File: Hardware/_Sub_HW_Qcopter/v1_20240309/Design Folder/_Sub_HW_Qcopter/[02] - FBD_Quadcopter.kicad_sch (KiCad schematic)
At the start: 0 parts

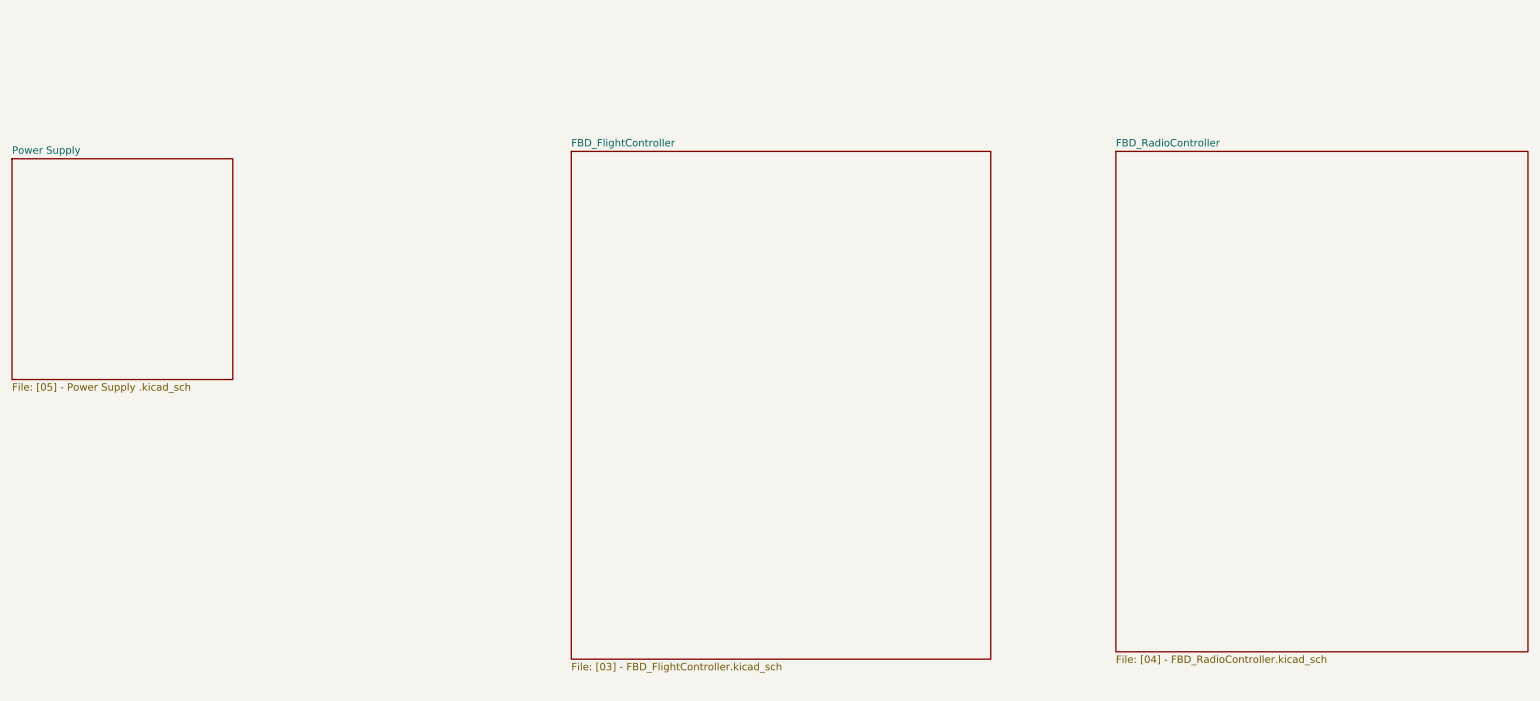
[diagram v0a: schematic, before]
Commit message: Schematic is done by 90%
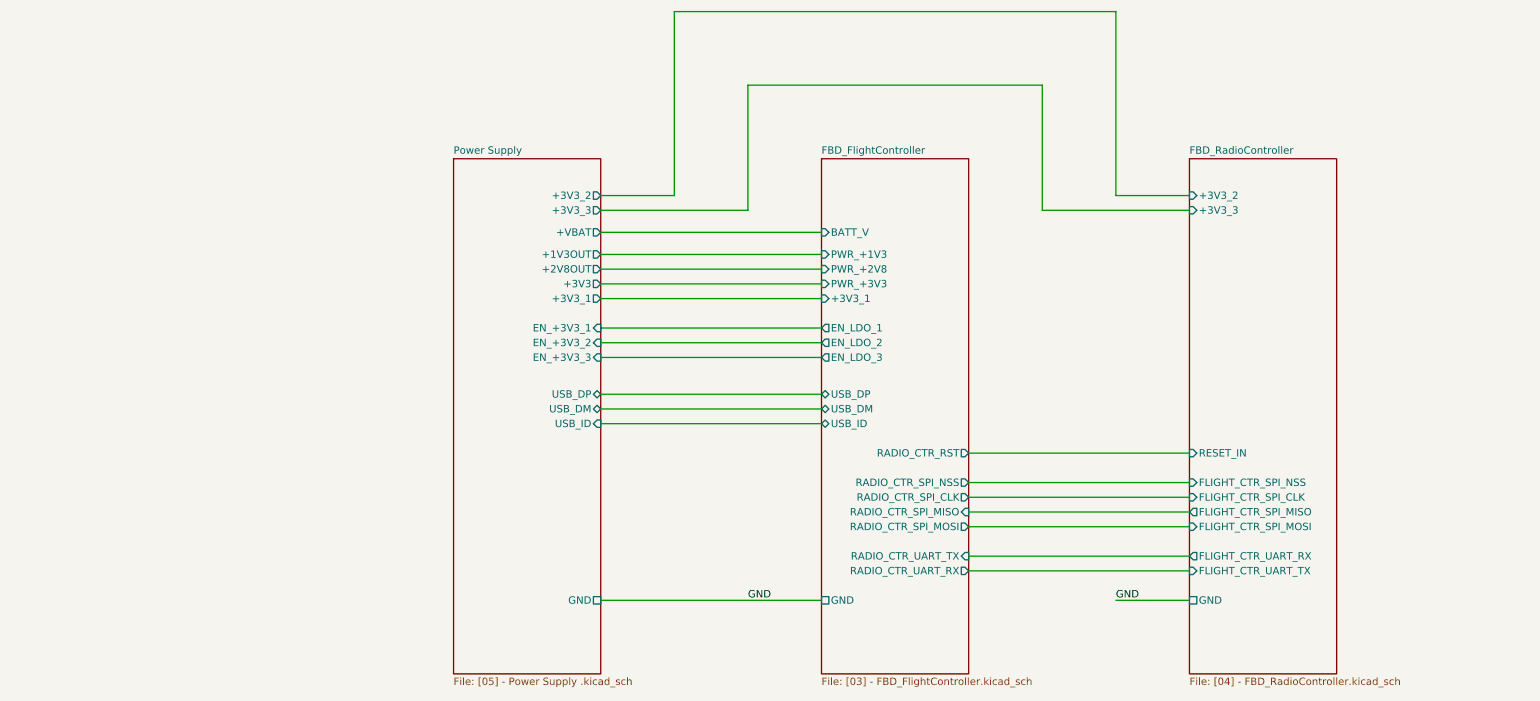
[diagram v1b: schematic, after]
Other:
- sheet FBD_FlightController ports: added +3V3_1, BATT_V, EN_LDO_1, EN_LDO_2, EN_LDO_3, GND, PWR_+1V3, PWR_+2V8, PWR_+3V3, RADIO_CTR_RST, RADIO_CTR_SPI_CLK, RADIO_CTR_SPI_MISO, RADIO_CTR_SPI_MOSI, RADIO_CTR_SPI_NSS, RADIO_CTR_UART_RX, RADIO_CTR_UART_TX, USB_DM, USB_DP, USB_ID; removed none
- sheet FBD_RadioController ports: added +3V3_2, +3V3_3, FLIGHT_CTR_SPI_CLK, FLIGHT_CTR_SPI_MISO, FLIGHT_CTR_SPI_MOSI, FLIGHT_CTR_SPI_NSS, FLIGHT_CTR_UART_RX, FLIGHT_CTR_UART_TX, GND, RESET_IN; removed none
- sheet Power Supply ports: added +1V3OUT, +2V8OUT, +3V3, +3V3_1, +3V3_2, +3V3_3, +VBAT, EN_+3V3_1, EN_+3V3_2, EN_+3V3_3, GND, USB_DM, USB_DP, USB_ID; removed none

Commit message: 97% drawing schematic is done
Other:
- sheet FBD_FlightController ports: added EN_LDO_4, EN_LDO_5, VM; removed none
- sheet Power Supply ports: added EN_+1V3, EN_+2V8, VM; removed none

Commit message: Update [02] - FBD_Quadcopter.kicad_sch
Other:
- sheet FBD_FlightController: file [03] - FBD_FlightController.kicad_sch -> [0201] - FBD_FlightController.kicad_sch
- sheet FBD_FlightController ports: added LDO_EN, PWR_+3V3_1; removed +3V3_1, GND, VM
- sheet FBD_RadioController: file [04] - FBD_RadioController.kicad_sch -> [0202] - FBD_RadioController.kicad_sch
- sheet FBD_RadioController ports: added none; removed GND
- sheet Power Supply: file [05] - Power Supply .kicad_sch -> [0203] - Power Supply .kicad_sch
- sheet Power Supply ports: added LDO_EN; removed GND, VM
- company: (none) -> Mend0z0
- title: (none) -> Quadcopter
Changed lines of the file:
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@@
 	(paper "C")
 	(title_block
-		(comment 2 "DRAFT")
+		(title "Quadcopter")
+		(date "2024-03-17")
+		(rev "01")
+		(company "Mend0z0")
+		(comment 1 "01")
+		(comment 2 "PRELIMINARY")
+		(comment 3 "Siavash Taher Parvar")
+		(comment 8 "N/A")
+		(comment 9 "First Version")
 	)
 	(wire
@@
 	(wire
 		(pts
-			(xy 203.2 153.67) (xy 241.3 153.67)
-		)
-		(stroke
-			(width 0)
-			(type default)
-		)
-	)
-	(wire
-		(pts
 			(xy 203.2 143.51) (xy 241.3 143.51)
 		)
@@
 	(wire
 		(pts
-			(xy 203.2 167.64) (xy 241.3 167.64)
-		)
-		(stroke
-			(width 0)
-			(type default)
-		)
-	)
-	(wire
-		(pts
-			(xy 203.2 160.02) (xy 241.3 160.02)
-		)
-		(stroke
-			(width 0)
-			(type default)
-		)
-	)
-	(wire
-		(pts
-			(xy 203.2 157.48) (xy 241.3 157.48)
+			(xy 203.2 171.45) (xy 241.3 171.45)
+		)
+		(stroke
+			(width 0)
+			(type default)
+		)
+	)
+	(wire
+		(pts
+			(xy 203.2 163.83) (xy 241.3 163.83)
+		)
+		(stroke
+			(width 0)
+			(type default)
+		)
+	)
+	(wire
+		(pts
+			(xy 203.2 161.29) (xy 241.3 161.29)
 		)
 		(stroke
@@
 	(wire
 		(pts
-			(xy 203.2 162.56) (xy 241.3 162.56)
+			(xy 203.2 166.37) (xy 241.3 166.37)
 		)
 		(stroke
@@
 	(wire
 		(pts
+			(xy 203.2 158.75) (xy 241.3 158.75)
+		)
+		(stroke
+			(width 0)
+			(type default)
+		)
+	)
+	(wire
+		(pts
 			(xy 266.7 196.85) (xy 304.8 196.85)
 		)
@@
 	(wire
 		(pts
-			(xy 203.2 172.72) (xy 241.3 172.72)
-		)
-		(stroke
-			(width 0)
-			(type default)
-		)
-	)
-	(wire
-		(pts
-			(xy 203.2 165.1) (xy 241.3 165.1)
+			(xy 203.2 176.53) (xy 241.3 176.53)
+		)
+		(stroke
+			(width 0)
+			(type default)
+		)
+	)
+	(wire
+		(pts
+			(xy 203.2 168.91) (xy 241.3 168.91)
 		)
 		(stroke
@@
 	(wire
 		(pts
-			(xy 292.1 212.09) (xy 304.8 212.09)
-		)
-		(stroke
-			(width 0)
-			(type default)
-		)
-	)
-	(wire
-		(pts
 			(xy 266.7 194.31) (xy 304.8 194.31)
 		)
@@
 	(wire
 		(pts
-			(xy 203.2 177.8) (xy 241.3 177.8)
-		)
-		(stroke
-			(width 0)
-			(type default)
-		)
-	)
-	(wire
-		(pts
-			(xy 203.2 210.82) (xy 241.3 210.82)
-		)
-		(stroke
-			(width 0)
-			(type default)
-		)
-	)
-	(wire
-		(pts
-			(xy 203.2 175.26) (xy 241.3 175.26)
-		)
-		(stroke
-			(width 0)
-			(type default)
-		)
-	)
-	(label "GND"
-		(at 292.1 212.09 0)
-		(fields_autoplaced yes)
+			(xy 203.2 181.61) (xy 241.3 181.61)
+		)
+		(stroke
+			(width 0)
+			(type default)
+		)
+	)
+	(wire
+		(pts
+			(xy 203.2 179.07) (xy 241.3 179.07)
+		)
+		(stroke
+			(width 0)
+			(type default)
+		)
+	)
+	(text_box "2"
+		(exclude_from_sim no)
+		(at 317.5 128.27 0)
+		(size 11.43 12.7)
+		(stroke
+			(width 0)
+			(type default)
+		)
+		(fill
+			(type none)
+		)
 		(effects
 			(font
-				(size 1.27 1.27)
-			)
-			(justify left bottom)
-		)
-	)
-	(label "GND"
-		(at 228.6 210.82 0)
-		(fields_autoplaced yes)
+				(size 5.08 5.08)
+				(thickness 1.016)
+				(bold yes)
+			)
+		)
+	)
+	(text_box "1"
+		(exclude_from_sim no)
+		(at 254 128.27 0)
+		(size 11.43 12.7)
+		(stroke
+			(width 0)
+			(type default)
+		)
+		(fill
+			(type none)
+		)
 		(effects
 			(font
-				(size 1.27 1.27)
-			)
-			(justify left bottom)
+				(size 5.08 5.08)
+				(thickness 1.016)
+				(bold yes)
+			)
+		)
+	)
+	(text_box "3"
+		(exclude_from_sim no)
+		(at 179.07 128.27 0)
+		(size 11.43 12.7)
+		(stroke
+			(width 0)
+			(type default)
+		)
+		(fill
+			(type none)
+		)
+		(effects
+			(font
+				(size 5.08 5.08)
+				(thickness 1.016)
+				(bold yes)
+			)
 		)
 	)
@@
 			)
 		)
-		(property "Sheetfile" "[05] - Power Supply .kicad_sch"
+		(property "Sheetfile" "[0203] - Power Supply .kicad_sch"
 			(at 177.8 216.4846 0)
 			(effects
@@
 		)
 		(pin "EN_+3V3_1" input
-			(at 203.2 157.48 0)
+			(at 203.2 161.29 0)
 			(effects
 				(font
@@
 		)
 		(pin "EN_+3V3_2" input
-			(at 203.2 160.02 0)
+			(at 203.2 163.83 0)
 			(effects
 				(font
@@
 		)
 		(pin "EN_+3V3_3" input
-			(at 203.2 162.56 0)
+			(at 203.2 166.37 0)
 			(effects
 				(font
@@
 		)
 		(pin "USB_DP" bidirectional
-			(at 203.2 172.72 0)
+			(at 203.2 176.53 0)
 			(effects
 				(font
@@
 		)
 		(pin "USB_DM" bidirectional
-			(at 203.2 175.26 0)
+			(at 203.2 179.07 0)
 			(effects
 				(font
@@
 		)
 		(pin "USB_ID" input
-			(at 203.2 177.8 0)
-			(effects
-				(font
-					(size 1.27 1.27)
-				)
-				(justify right)
-			)
-		)
-		(pin "GND" passive
-			(at 203.2 210.82 0)
+			(at 203.2 181.61 0)
 			(effects
 				(font
@@
 		)
 		(pin "EN_+1V3" input
-			(at 203.2 165.1 0)
+			(at 203.2 168.91 0)
 			(effects
 				(font
@@
 		)
 		(pin "EN_+2V8" input
-			(at 203.2 167.64 0)
-			(effects
-				(font
-					(size 1.27 1.27)
-				)
-				(justify right)
-			)
-		)
-		(pin "VM" output
-			(at 203.2 153.67 0)
+			(at 203.2 171.45 0)
+			(effects
+				(font
+					(size 1.27 1.27)
+				)
+				(justify right)
+			)
+		)
+		(pin "LDO_EN" input
+			(at 203.2 158.75 0)
 			(effects
 				(font
@@
 			(project "_Sub_HW_Qcopter"
 				(path "/b8703f06-b3da-4de2-b217-f104939b36e8/6184e84e-040e-4878-8152-76cf0b949e21"
-					(page "22")
+					(page "5")
 				)
 			)
@@
 			)
 		)
-		(property "Sheetfile" "[04] - FBD_RadioController.kicad_sch"
+		(property "Sheetfile" "[0202] - FBD_RadioController.kicad_sch"
 			(at 304.8 216.4846 0)
 			(effects
@@
 		(pin "+3V3_3" input
 			(at 304.8 135.89 180)
-			(effects
-				(font
-					(size 1.27 1.27)
-				)
-				(justify left)
-			)
-		)
-		(pin "GND" passive
-			(at 304.8 212.09 180)
 			(effects
 				(font
@@
 			)
 		)
-		(property "Sheetfile" "[03] - FBD_FlightController.kicad_sch"
+		(property "Sheetfile" "[0201] - FBD_FlightController.kicad_sch"
 			(at 241.3 216.4846 0)
 			(effects
@@
 		)
 		(pin "EN_LDO_1" output
-			(at 241.3 157.48 180)
+			(at 241.3 161.29 180)
 			(effects
 				(font
@@
 		)
 		(pin "EN_LDO_2" output
-			(at 241.3 160.02 180)
+			(at 241.3 163.83 180)
 			(effects
 				(font
@@
 		)
 		(pin "EN_LDO_3" output
-			(at 241.3 162.56 180)
+			(at 241.3 166.37 180)
 			(effects
 				(font
@@
 		)
 		(pin "USB_DP" bidirectional
-			(at 241.3 172.72 180)
+			(at 241.3 176.53 180)
 			(effects
 				(font
@@
 		)
 		(pin "USB_DM" bidirectional
-			(at 241.3 175.26 180)
+			(at 241.3 179.07 180)
 			(effects
 				(font
@@
 		)
 		(pin "USB_ID" bidirectional
-			(at 241.3 177.8 180)
-			(effects
-				(font
-					(size 1.27 1.27)
-				)
-				(justify left)
-			)
-		)
-		(pin "GND" passive
-			(at 241.3 210.82 180)
+			(at 241.3 181.61 180)
 			(effects
 				(font
@@
 			)
 		)
-		(pin "+3V3_1" input
-			(at 241.3 151.13 180)
-			(effects
-				(font
-					(size 1.27 1.27)
-				)
-				(justify left)
-			)
-		)
 		(pin "PWR_+1V3" input
 			(at 241.3 143.51 180)
@@
 		)
 		(pin "EN_LDO_4" output
-			(at 241.3 165.1 180)
+			(at 241.3 168.91 180)
 			(effects
 				(font
@@
 		)
 		(pin "EN_LDO_5" output
-			(at 241.3 167.64 180)
-			(effects
-				(font
-					(size 1.27 1.27)
-				)
-				(justify left)
-			)
-		)
-		(pin "VM" input
-			(at 241.3 153.67 180)
-			(effects
-				(font
+			(at 241.3 171.45 180)
+			(effects
+				(font
+					(size 1.27 1.27)
+				)
+				(justify left)
+			)
+		)
+		(pin "LDO_EN" output
+			(at 241.3 158.75 180)
+			(effects
+				(font
+					(size 1.27 1.27)
+				)
+				(justify left)
+			)
+		)
+		(pin "PWR_+3V3_1" input
+			(at 241.3 151.13 180)
+			(effects
+				(font

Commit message: Update [02] - FBD_Quadcopter.kicad_sch
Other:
- sheet Power Supply ports: added +1V3, +2V8; removed +1V3OUT, +2V8OUT
- note added: "CHECKED"
